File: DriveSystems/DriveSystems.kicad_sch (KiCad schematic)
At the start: 12 parts, among them J1 Raspberry_Pi_4, U1 RoboClaw Motor Controller, U2 5304 Gear Motor, U3 24VDC UBC-C PSU

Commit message: Cleanup & New things
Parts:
- removed F2: 30A Fuse, symbol Device:Fuse
- removed Off/On1: RotaryEncoder_Switch, symbol Device:RotaryEncoder_Switch
- added M1, M2: Motor_Servo, symbol Motor:Motor_Servo
- added R1, R2, R3, R4, R5: 10k, symbol Device:R
- added RideStop: SW_Push_LED, symbol Switch:SW_Push_LED
- added SW1: SW_Rotary_1x2_MP, symbol Switch:SW_Rotary_1x3_MP
- added U4: 24V 5V10A DCDC Stepdown, symbol CustomSymbols:24V 5V10A_DCDC_Stepdown
- added U5: RoboClaw VClamp, symbol CustomSymbols:RoboclawVClamp
- added U6: Pwr Res, symbol CustomSymbols:Power_Resistor
- CB1: value CircuitBreaker_1P -> 30 Circuit Breaker
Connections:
- net at J1.11 (GPIO17/SPI1_~{CE1}): now also R4.1, SW1.3
- net at J1.12 (GPIO18/SPI1_~{CE0}/PCM_CLK/PWM0): now also Dispatch2.1, R3.1
- net at J1.14 (GND), J1.20 (GND), J1.25 (GND)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: now also R1.2, R2.2, R3.2, R4.2, R5.2; no longer Dispatch1.4 (A), Dispatch2.4 (A), Estop1.2, Restart1.4 (A)
- net at J1.32 (GPIO12/PWM0): now also M2.1 (PWM)
- net at J1.33 (GPIO13/PWM1): now also M1.1 (PWM)
- net at J1.35 (GPIO19/SPI1_MISO/PCM_FS): now also Restart1.1, R2.1; no longer Dispatch1.3 (K)
- net at J1.36 (GPIO16/SPI1_~{CE2}): now also R5.1, SW1.2
- net at J1.38 (GPIO20/SPI1_MOSI/PCM_DIN/PWM1): now also R1.1, RideStop.1; no longer Restart1.3 (K)
- net at J1.40 (GPIO21/SPI1_SCLK/PCM_DOUT): no longer Dispatch2.3 (K)
- net at J1.7 (GPCLK0/GPIO04): now also U1.S5 (Brake)
- net at U1. (5VDC): now also U2.6 (Ch_B)
- net at U1. (5VDC), U2.3 (VCC): now also U5.2 (+5V)
- net at U1. (5VDC), U2.4 (GND): now also U5.3 (GND)
- net at CB1.1, U1.3 (Vin+): now also U4.1 (24Vin), U5.5 (V+)
- net at U1.4 (Vin-), U3.2 (GND): now also U4.2 (GND), U5.4 (GND)
- net at U1.S3 (VClamp): now also U5.1 (CTRL)
- net at Dispatch1.1: now also Dispatch2.2
- new net: Dispatch1.2, Estop1.1, J1.1 (3V3), J1.17 (3V3), Restart1.2, RideStop.2, SW1.1
- new net: Estop1.2, U1.S4 (E-STOP)
- new net: M1.2 (+), M2.2 (+), U4.3 (5Vout)
- new net: M1.3 (-), M2.3 (-), U4.4 (GND)
- new net: U5.6 (R1_A), U6.2
- new net: U5.7 (R1_B), U6.1
- now unconnected: J1.13 (GPIO27/SDIO_DAT3), J1.16 (GPIO23/SDIO_CMD), J1.18 (GPIO24/SDIO_DAT0), J1.37 (GPIO26/SDIO_DAT2)
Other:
- note added: "12AWG Wago Terminal ->"
- note added: "12AWG Wire"
- note added: "16AWG Wire"
- note added: "<- 12AWG Wago Terminal"
- note added: "Pull-Down Resistors"
- moved on the sheet: CB1, Dispatch1, Dispatch2, Estop1A, F1, Restart1, U1, U2, U3

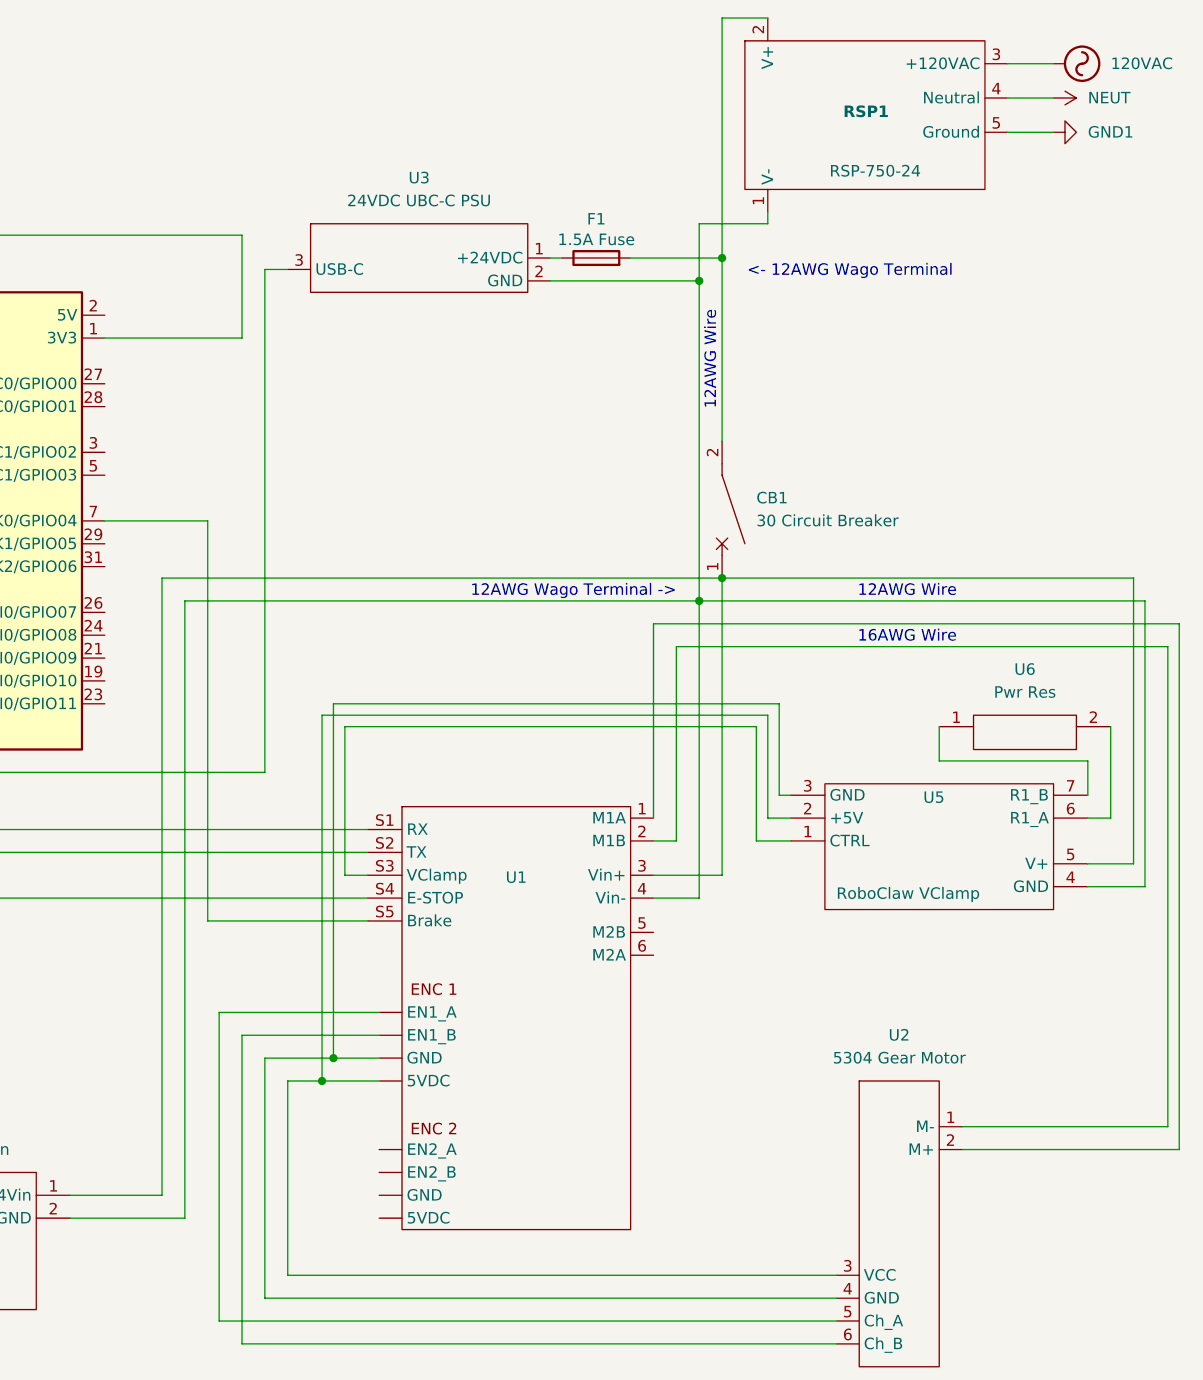
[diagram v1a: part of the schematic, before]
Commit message: Updated title block
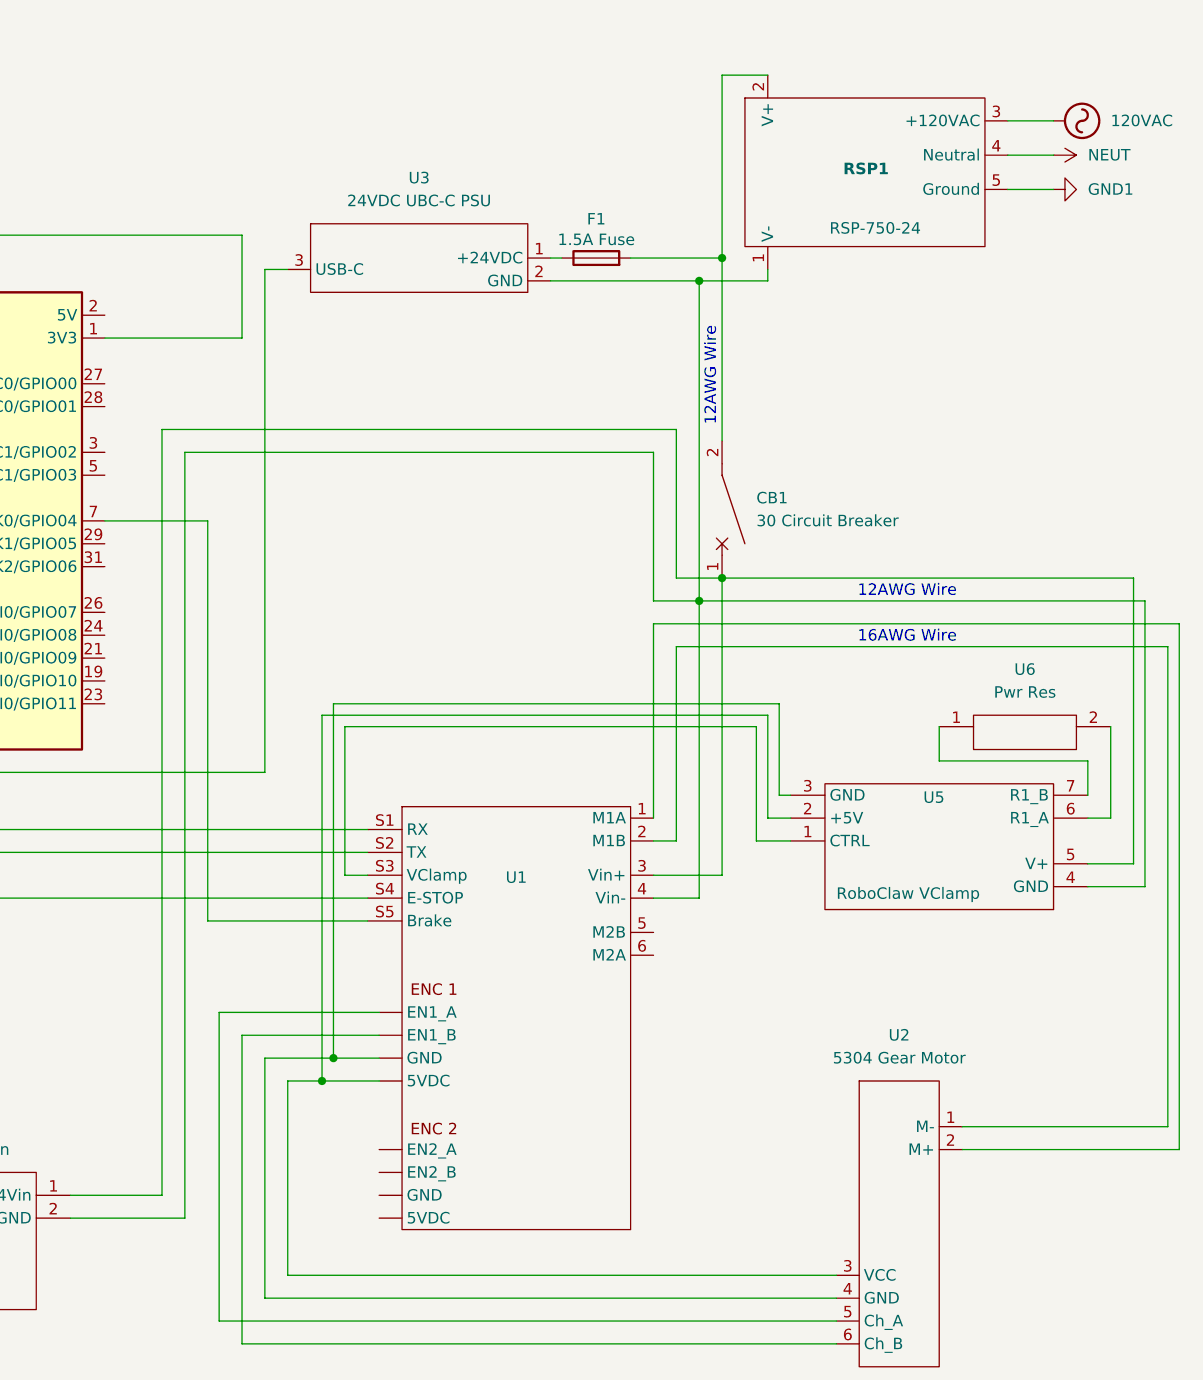
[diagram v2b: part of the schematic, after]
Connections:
- net at U1. (5VDC): now also U2.6 (Ch_B)
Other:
- note removed: "12AWG Wago Terminal ->"
- note removed: "<- 12AWG Wago Terminal"
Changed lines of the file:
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@@
 	(title_block
 		(title "REC 2025 ELECTRONIC SCHEMATIC")
-		(date "2025-02-25")
-		(rev "C")
+		(date "2025-03-03")
+		(rev "D")
 		(company "TERRIER RIDE ENGINEERING CLUB")
-		(comment 1 "PRELIMINARY")
-	)
-	(text "12AWG Wago Terminal ->"
-		(exclude_from_sim no)
-		(at 217.17 77.724 0)
-		(effects
-			(font
-				(size 1.27 1.27)
-			)
-		)
+		(comment 1 "FINAL CANIDATE")
+		(comment 2 "Contributer: Jack Justus")
+		(comment 3 "Contributer: Jesus Espinoza")
 	)
 	(text "Pin 1 represents NC\nPin 2 represents NO  \nPin 3 represents (-)L2 light terminal\nPin 4 represents (+)L2 light terminal"
@@
 		)
 	)
-	(text "<- 12AWG Wago Terminal"
-		(exclude_from_sim no)
-		(at 247.904 42.164 0)
-		(effects
-			(font
-				(size 1.27 1.27)
-			)
-		)
-	)
 	(text "12AWG Wire"
 		(exclude_from_sim no)
-		(at 232.41 52.07 90)
+		(at 232.41 53.848 90)
 		(effects
 			(font
@@
 	(wire
 		(pts
+			(xy 173.99 62.23) (xy 173.99 147.32)
+		)
+		(stroke
+			(width 0)
+			(type default)
+		)
+	)
+	(wire
+		(pts
 			(xy 15.24 50.8) (xy 15.24 57.15)
 		)
@@
 	(wire
 		(pts
-			(xy 265.43 19.05) (xy 270.51 19.05)
+			(xy 265.43 25.4) (xy 270.51 25.4)
 		)
 		(stroke
@@
 	(wire
 		(pts
-			(xy 233.68 13.97) (xy 233.68 40.64)
+			(xy 233.68 20.32) (xy 233.68 40.64)
 		)
 		(stroke
@@
 	(wire
 		(pts
+			(xy 228.6 76.2) (xy 228.6 59.69)
+		)
+		(stroke
+			(width 0)
+			(type default)
+		)
+	)
+	(wire
+		(pts
 			(xy 55.88 82.55) (xy 55.88 97.79)
 		)
@@
 	(wire
 		(pts
-			(xy 173.99 147.32) (xy 173.99 78.74)
+			(xy 231.14 43.18) (xy 231.14 78.74)
 		)
 		(stroke
@@
 	(wire
 		(pts
-			(xy 231.14 43.18) (xy 231.14 78.74)
+			(xy 226.06 111.76) (xy 231.14 111.76)
 		)
 		(stroke
@@
 	(wire
 		(pts
-			(xy 226.06 111.76) (xy 231.14 111.76)
+			(xy 107.95 165.1) (xy 107.95 170.18)
 		)
 		(stroke
@@
 	(wire
 		(pts
-			(xy 107.95 165.1) (xy 107.95 170.18)
+			(xy 92.71 130.81) (xy 114.3 130.81)
 		)
 		(stroke
@@
 	(wire
 		(pts
-			(xy 92.71 130.81) (xy 114.3 130.81)
+			(xy 55.88 69.85) (xy 59.69 69.85)
 		)
 		(stroke
@@
 	(wire
 		(pts
-			(xy 55.88 69.85) (xy 59.69 69.85)
+			(xy 171.45 59.69) (xy 228.6 59.69)
 		)
 		(stroke
@@
 	(wire
 		(pts
+			(xy 228.6 76.2) (xy 233.68 76.2)
+		)
+		(stroke
+			(width 0)
+			(type default)
+		)
+	)
+	(wire
+		(pts
 			(xy 137.16 160.02) (xy 114.3 160.02)
 		)
@@
 	(wire
 		(pts
-			(xy 265.43 22.86) (xy 270.51 22.86)
+			(xy 265.43 29.21) (xy 270.51 29.21)
+		)
+		(stroke
+			(width 0)
+			(type default)
+		)
+	)
+	(wire
+		(pts
+			(xy 226.06 78.74) (xy 226.06 62.23)
 		)
 		(stroke
@@
 	(wire
 		(pts
-			(xy 265.43 26.67) (xy 270.51 26.67)
+			(xy 265.43 33.02) (xy 270.51 33.02)
 		)
 		(stroke
@@
 	(wire
 		(pts
-			(xy 233.68 13.97) (xy 238.76 13.97)
+			(xy 233.68 20.32) (xy 238.76 20.32)
 		)
 		(stroke
@@
 	(wire
 		(pts
-			(xy 238.76 35.56) (xy 238.76 36.83)
+			(xy 238.76 41.91) (xy 238.76 43.18)
 		)
 		(stroke
@@
 	(wire
 		(pts
-			(xy 171.45 76.2) (xy 233.68 76.2)
+			(xy 214.63 43.18) (xy 231.14 43.18)
 		)
 		(stroke
@@
 	(wire
 		(pts
-			(xy 214.63 43.18) (xy 231.14 43.18)
+			(xy 15.24 38.1) (xy 15.24 50.8)
 		)
 		(stroke
@@
 	(wire
 		(pts
-			(xy 15.24 38.1) (xy 15.24 50.8)
+			(xy 240.03 100.33) (xy 240.03 90.17)
 		)
 		(stroke
@@
 	(wire
 		(pts
-			(xy 240.03 100.33) (xy 240.03 90.17)
+			(xy 240.03 90.17) (xy 190.5 90.17)
 		)
 		(stroke
@@
 	(wire
 		(pts
-			(xy 240.03 90.17) (xy 190.5 90.17)
+			(xy 173.99 62.23) (xy 226.06 62.23)
 		)
 		(stroke
@@
 	(wire
 		(pts
-			(xy 173.99 78.74) (xy 231.14 78.74)
-		)
-		(stroke
-			(width 0)
-			(type default)
-		)
-	)
-	(wire
-		(pts
 			(xy 43.18 62.23) (xy 82.55 62.23)
 		)
@@
 	(wire
 		(pts
-			(xy 171.45 76.2) (xy 171.45 144.78)
+			(xy 171.45 59.69) (xy 171.45 144.78)
 		)
 		(stroke
@@
 	(wire
 		(pts
-			(xy 231.14 36.83) (xy 238.76 36.83)
+			(xy 231.14 43.18) (xy 238.76 43.18)
 		)
 		(stroke
@@
 	(wire
 		(pts
-			(xy 231.14 36.83) (xy 231.14 43.18)
+			(xy 226.06 78.74) (xy 231.14 78.74)
 		)
 		(stroke
@@
 	(symbol
 		(lib_id "CustomSymbols:RSP-750-24")
-		(at 254 24.13 0)
+		(at 254 30.48 0)
 		(unit 1)
 		(exclude_from_sim no)
@@
 		(dnp no)
 		(property "Reference" "RSP1"
-			(at 252.222 24.384 0)
+			(at 252.222 30.734 0)
 			(effects
 				(font
@@
 		)
 		(property "Value" "RSP-750-24"
-			(at 255.778 30.988 0)
+			(at 255.778 37.338 0)
 			(effects
 				(font
@@
 		)
 		(property "Footprint" ""
-			(at 251.46 17.78 0)
+			(at 251.46 24.13 0)
 			(effects
 				(font
@@
 		)
 		(property "Datasheet" ""
-			(at 251.46 17.78 0)
+			(at 251.46 24.13 0)
 			(effects
 				(font
@@
 		)
 		(property "Description" ""
-			(at 251.46 17.78 0)
+			(at 251.46 24.13 0)
 			(effects
 				(font
@@
 	(symbol
 		(lib_id "power:VAC")
-		(at 270.51 19.05 270)
+		(at 270.51 25.4 270)
 		(unit 1)
 		(exclude_from_sim no)
@@
 		(dnp no)
 		(property "Reference" "#PWR01"
-			(at 267.97 19.05 0)
+			(at 267.97 25.4 0)
 			(effects
 				(font
@@
 		)
 		(property "Value" "120VAC"
-			(at 276.86 19.0499 90)
+			(at 276.86 25.3999 90)
 			(effects
 				(font
@@
 		)
 		(property "Footprint" ""
-			(at 270.51 19.05 0)
+			(at 270.51 25.4 0)
 			(effects
 				(font
@@
 		)
 		(property "Datasheet" ""
-			(at 270.51 19.05 0)
+			(at 270.51 25.4 0)
 			(effects
 				(font
@@
 		)
 		(property "Description" "Power symbol creates a global label with name \"VAC\""
-			(at 270.51 19.05 0)
+			(at 270.51 25.4 0)
 			(effects
 				(font
@@
 	(symbol
 		(lib_id "power:NEUT")
-		(at 270.51 22.86 270)
+		(at 270.51 29.21 270)
 		(unit 1)
 		(exclude_from_sim no)
@@
 		(dnp no)
 		(property "Reference" "#PWR013"
-			(at 266.7 22.86 0)
+			(at 266.7 29.21 0)
 			(effects
 				(font
@@
 		)
 		(property "Value" "NEUT"
-			(at 274.32 22.8599 90)
+			(at 274.32 29.2099 90)
 			(effects
 				(font
@@
 		)
 		(property "Footprint" ""
-			(at 270.51 22.86 0)
+			(at 270.51 29.21 0)
 			(effects
 				(font
@@
 		)
 		(property "Datasheet" ""
-			(at 270.51 22.86 0)
+			(at 270.51 29.21 0)
 			(effects
 				(font
@@
 		)
 		(property "Description" "Power symbol creates a global label with name \"NEUT\""
-			(at 270.51 22.86 0)
+			(at 270.51 29.21 0)
 			(effects
 				(font
@@
 	(symbol
 		(lib_id "power:GND1")
-		(at 270.51 26.67 90)
+		(at 270.51 33.02 90)
 		(unit 1)
 		(exclude_from_sim no)
@@
 		(dnp no)
 		(property "Reference" "#PWR012"
-			(at 276.86 26.67 0)
+			(at 276.86 33.02 0)
 			(effects
 				(font
@@
 		)
 		(property "Value" "GND1"
-			(at 274.32 26.6699 90)
+			(at 274.32 33.0199 90)
 			(effects
 				(font
@@
 		)
 		(property "Footprint" ""
-			(at 270.51 26.67 0)
+			(at 270.51 33.02 0)
 			(effects
 				(font
@@
 		)
 		(property "Datasheet" ""
-			(at 270.51 26.67 0)
+			(at 270.51 33.02 0)
 			(effects
 				(font
@@
 		)
 		(property "Description" "Power symbol creates a global label with name \"GND1\" , ground"
-			(at 270.51 26.67 0)
+			(at 270.51 33.02 0)
 			(effects
 				(font
